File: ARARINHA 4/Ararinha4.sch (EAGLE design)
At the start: 105 parts, among them IC1 4053N, Q1 BC548, Q2 BC548, Q3 BC548, Q4 BC548, Q5 BC548, Q6 BC548, T1 TOROID-T37-4PIN, T2 TOROID-T37-4PIN, U1 LM386

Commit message: Adicionado o PA do Ararinha 4 pronto para transferência termica (ainda passível de testes); primeiras partes da mainboard do Ararinha 4 sendo desenhadas.
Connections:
- net GND: now also C22.1, TR1.7, TR2.6; no longer C22.2, XTAL2.GND, XTAL3.GND, XTAL4.GND, XTAL5.GND
- net N$28: now also C22.2; no longer C22.1
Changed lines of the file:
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@@
 <part name="JP5" library="pinhead" deviceset="PINHD-1X2" device="" value="TXOUT"/>
 <part name="SUPPLY35" library="supply2" deviceset="GND" device=""/>
+<part name="SUPPLY36" library="supply2" deviceset="GND" device=""/>
+<part name="SUPPLY37" library="supply2" deviceset="GND" device=""/>
 </parts>
 <sheets>
@@
 <instance part="JP5" gate="G$1" x="-147.32" y="43.18" rot="R180"/>
 <instance part="SUPPLY35" gate="GND" x="-137.16" y="35.56"/>
+<instance part="SUPPLY36" gate="GND" x="-116.84" y="-7.62"/>
+<instance part="SUPPLY37" gate="GND" x="-43.18" y="-7.62"/>
 </instances>
 <busses>
@@
 </segment>
 <segment>
-<pinref part="XTAL4" gate="G$1" pin="GND"/>
-<wire x1="185.42" y1="27.94" x2="185.42" y2="17.78" width="0.1524" layer="91"/>
-<wire x1="185.42" y1="17.78" x2="182.88" y2="15.24" width="0.1524" layer="91"/>
-<pinref part="C22" gate="G$1" pin="2"/>
-<wire x1="182.88" y1="15.24" x2="177.8" y2="15.24" width="0.1524" layer="91"/>
+<pinref part="C22" gate="G$1" pin="1"/>
+<wire x1="182.88" y1="15.24" x2="177.8" y2="22.86" width="0.1524" layer="91"/>
 <pinref part="SUPPLY20" gate="GND" pin="GND"/>
-<wire x1="177.8" y1="15.24" x2="167.64" y2="15.24" width="0.1524" layer="91"/>
-<wire x1="167.64" y1="15.24" x2="165.1" y2="15.24" width="0.1524" layer="91"/>
+<wire x1="177.8" y1="22.86" x2="165.1" y2="15.24" width="0.1524" layer="91"/>
 <wire x1="165.1" y1="15.24" x2="162.56" y2="12.7" width="0.1524" layer="91"/>
-<pinref part="XTAL5" gate="G$1" pin="GND"/>
-<wire x1="139.7" y1="27.94" x2="139.7" y2="20.32" width="0.1524" layer="91"/>
-<wire x1="139.7" y1="20.32" x2="144.78" y2="15.24" width="0.1524" layer="91"/>
 <pinref part="C21" gate="G$1" pin="2"/>
 <wire x1="144.78" y1="15.24" x2="147.32" y2="15.24" width="0.1524" layer="91"/>
 <wire x1="162.56" y1="12.7" x2="160.02" y2="15.24" width="0.1524" layer="91"/>
-<wire x1="160.02" y1="15.24" x2="157.48" y2="15.24" width="0.1524" layer="91"/>
-<pinref part="XTAL2" gate="G$1" pin="GND"/>
-<wire x1="157.48" y1="15.24" x2="147.32" y2="15.24" width="0.1524" layer="91"/>
-<wire x1="154.94" y1="27.94" x2="157.48" y2="25.4" width="0.1524" layer="91"/>
-<wire x1="157.48" y1="25.4" x2="157.48" y2="15.24" width="0.1524" layer="91"/>
-<pinref part="XTAL3" gate="G$1" pin="GND"/>
-<wire x1="170.18" y1="27.94" x2="167.64" y2="25.4" width="0.1524" layer="91"/>
-<wire x1="167.64" y1="25.4" x2="167.64" y2="15.24" width="0.1524" layer="91"/>
+<wire x1="160.02" y1="15.24" x2="147.32" y2="15.24" width="0.1524" layer="91"/>
 </segment>
 <segment>
@@
 <wire x1="-144.78" y1="40.64" x2="-139.7" y2="40.64" width="0.1524" layer="91"/>
 <wire x1="-139.7" y1="40.64" x2="-137.16" y2="38.1" width="0.1524" layer="91"/>
+</segment>
+<segment>
+<pinref part="TR1" gate="TR" pin="7"/>
+<pinref part="SUPPLY36" gate="GND" pin="GND"/>
+</segment>
+<segment>
+<pinref part="TR2" gate="TR" pin="6"/>
+<pinref part="SUPPLY37" gate="GND" pin="GND"/>
 </segment>
 </net>
@@
 <pinref part="XTAL4" gate="G$1" pin="2"/>
 <wire x1="172.72" y1="33.02" x2="177.8" y2="33.02" width="0.1524" layer="91"/>
-<pinref part="C22" gate="G$1" pin="1"/>
+<pinref part="C22" gate="G$1" pin="2"/>
 <wire x1="177.8" y1="33.02" x2="182.88" y2="33.02" width="0.1524" layer="91"/>
-<wire x1="177.8" y1="22.86" x2="177.8" y2="33.02" width="0.1524" layer="91"/>
-</segment>
-</net>
+<wire x1="177.8" y1="15.24" x2="177.8" y2="33.02" width="0.1524" layer="91"/>
+</segment>
+</net>

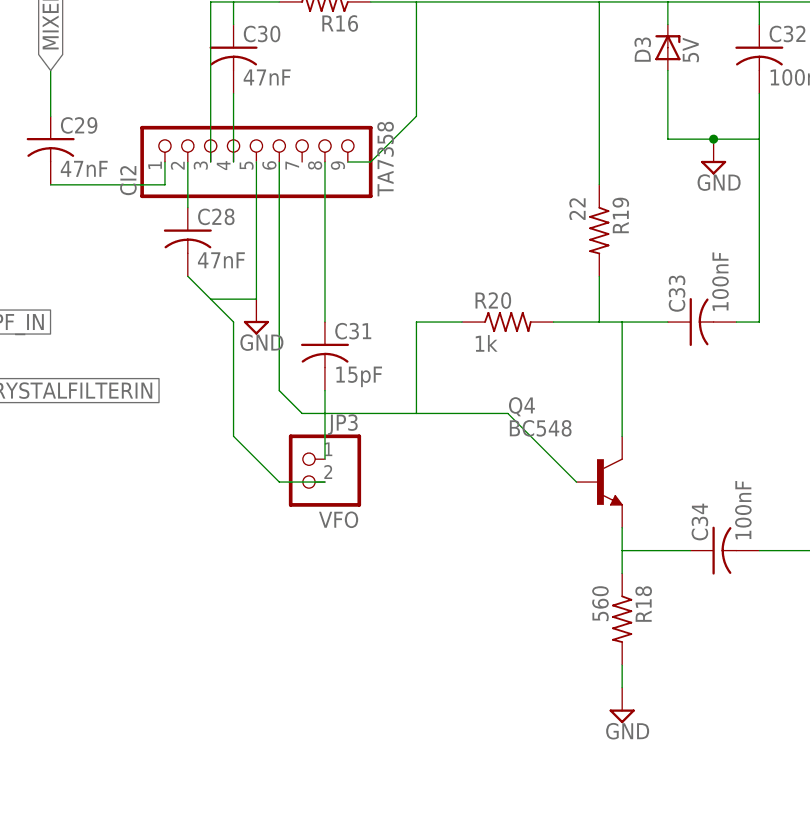
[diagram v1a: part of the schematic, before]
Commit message: 
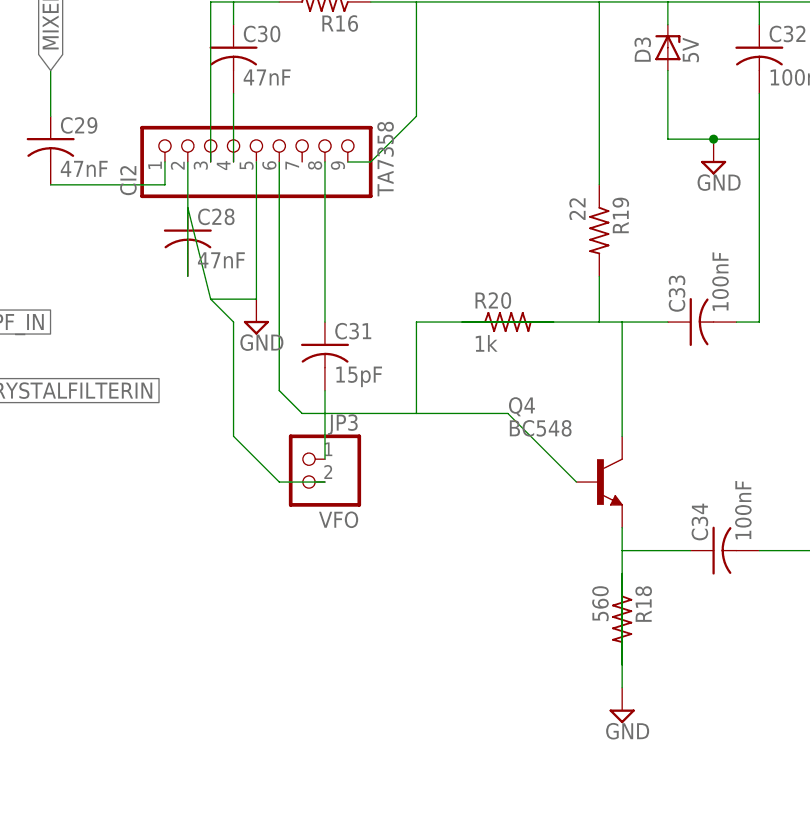
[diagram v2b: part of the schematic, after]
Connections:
- net GND: now also C28.1, R18.1; no longer C28.2, R18.2
- net N$30: now also C28.2; no longer C28.1
- net N$41: now also R18.2; no longer R18.1
- net N$42: now also R20.2; no longer R20.1
- net N$44: now also R20.1; no longer R20.2
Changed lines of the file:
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@@
 <pinref part="SUPPLY22" gate="GND" pin="GND"/>
 <wire x1="-33.02" y1="-76.2" x2="-33.02" y2="-60.96" width="0.1524" layer="91"/>
-<pinref part="C28" gate="G$1" pin="2"/>
-<wire x1="-40.64" y1="-73.66" x2="-38.1" y2="-76.2" width="0.1524" layer="91"/>
+<pinref part="C28" gate="G$1" pin="1"/>
+<wire x1="-40.64" y1="-66.04" x2="-38.1" y2="-76.2" width="0.1524" layer="91"/>
 <wire x1="-38.1" y1="-76.2" x2="-33.02" y2="-76.2" width="0.1524" layer="91"/>
 <pinref part="JP3" gate="G$1" pin="2"/>
@@
 </segment>
 <segment>
-<pinref part="R18" gate="G$1" pin="2"/>
+<pinref part="R18" gate="G$1" pin="1"/>
 <pinref part="SUPPLY24" gate="GND" pin="GND"/>
-<wire x1="7.62" y1="-119.38" x2="7.62" y2="-116.84" width="0.1524" layer="91"/>
+<wire x1="7.62" y1="-119.38" x2="7.62" y2="-106.68" width="0.1524" layer="91"/>
 </segment>
 <segment>
@@
 <segment>
 <pinref part="CI2" gate="A" pin="2"/>
-<pinref part="C28" gate="G$1" pin="1"/>
-<wire x1="-40.64" y1="-66.04" x2="-40.64" y2="-60.96" width="0.1524" layer="91"/>
+<pinref part="C28" gate="G$1" pin="2"/>
+<wire x1="-40.64" y1="-73.66" x2="-40.64" y2="-60.96" width="0.1524" layer="91"/>
 </segment>
 </net>
@@
 <segment>
 <pinref part="Q4" gate="G$1" pin="E"/>
-<pinref part="R18" gate="G$1" pin="1"/>
-<wire x1="7.62" y1="-106.68" x2="7.62" y2="-104.14" width="0.1524" layer="91"/>
+<pinref part="R18" gate="G$1" pin="2"/>
+<wire x1="7.62" y1="-116.84" x2="7.62" y2="-104.14" width="0.1524" layer="91"/>
 <pinref part="C34" gate="G$1" pin="1"/>
 <wire x1="7.62" y1="-104.14" x2="7.62" y2="-101.6" width="0.1524" layer="91"/>
@@
 <wire x1="-15.24" y1="-88.9" x2="-5.08" y2="-88.9" width="0.1524" layer="91"/>
 <wire x1="-5.08" y1="-88.9" x2="2.54" y2="-96.52" width="0.1524" layer="91"/>
+<pinref part="R20" gate="G$1" pin="2"/>
+<wire x1="0" y1="-78.74" x2="-15.24" y2="-78.74" width="0.1524" layer="91"/>
+<wire x1="-15.24" y1="-78.74" x2="-15.24" y2="-88.9" width="0.1524" layer="91"/>
+</segment>
+</net>
+<net name="N$44" class="0">
+<segment>
+<pinref part="C33" gate="G$1" pin="1"/>
 <pinref part="R20" gate="G$1" pin="1"/>
-<wire x1="-10.16" y1="-78.74" x2="-15.24" y2="-78.74" width="0.1524" layer="91"/>
-<wire x1="-15.24" y1="-78.74" x2="-15.24" y2="-88.9" width="0.1524" layer="91"/>
-</segment>
-</net>
-<net name="N$44" class="0">
-<segment>
-<pinref part="C33" gate="G$1" pin="1"/>
-<pinref part="R20" gate="G$1" pin="2"/>
-<wire x1="0" y1="-78.74" x2="5.08" y2="-78.74" width="0.1524" layer="91"/>
+<wire x1="-10.16" y1="-78.74" x2="5.08" y2="-78.74" width="0.1524" layer="91"/>
 <pinref part="R19" gate="G$1" pin="2"/>
 <wire x1="5.08" y1="-78.74" x2="7.62" y2="-78.74" width="0.1524" layer="91"/>
